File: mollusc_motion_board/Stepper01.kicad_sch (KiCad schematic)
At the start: 7 parts, among them J4 RJ45 x4, U1 SN74AHCT125N, U4 74HC14

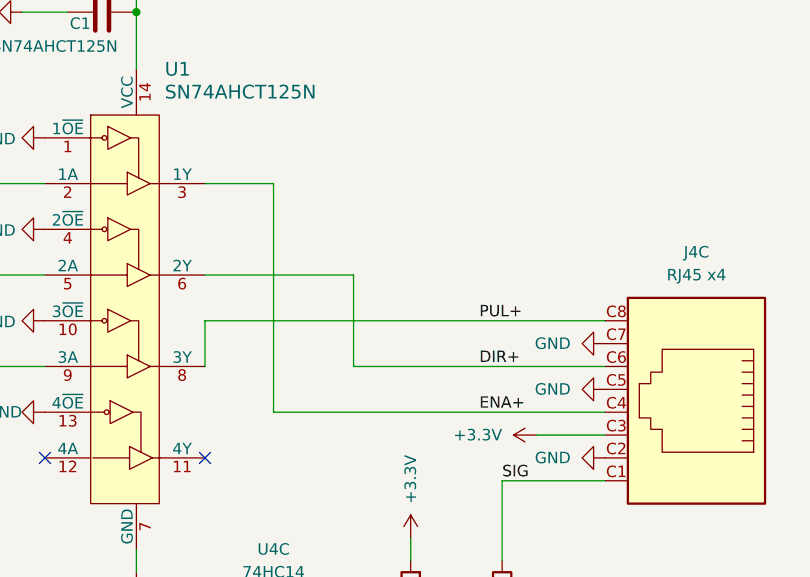
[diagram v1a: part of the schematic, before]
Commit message: adding ethernet jack
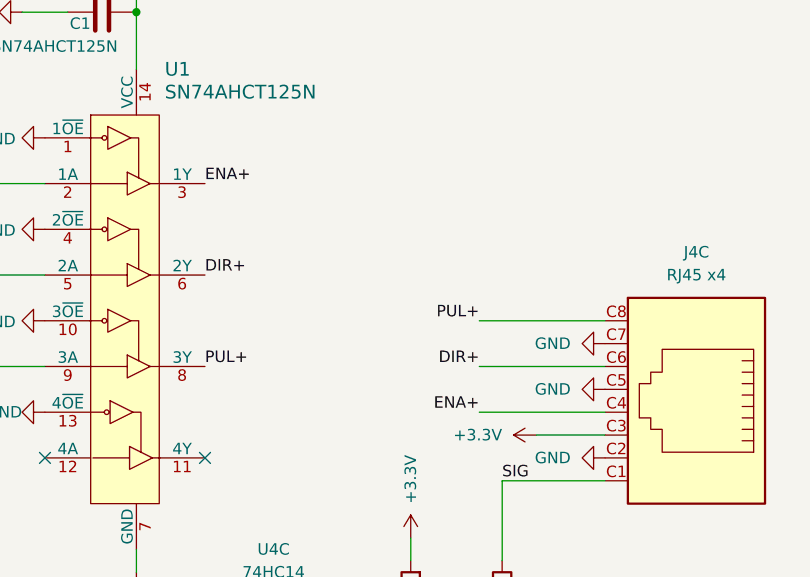
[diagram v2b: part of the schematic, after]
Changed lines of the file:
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@@
   (no_connect (at 166.37 107.95))
   (no_connect (at 148.59 107.95))
-  (wire (pts (xy 166.37 92.71) (xy 166.37 97.79))
-    (stroke (width 0) (type default))
-  )
   (wire (pts (xy 146.05 58.42) (xy 151.13 58.42))
-    (stroke (width 0) (type default))
-  )
-  (wire (pts (xy 173.99 102.87) (xy 210.82 102.87))
     (stroke (width 0) (type default))
   )
@@
     (stroke (width 0) (type default))
   )
+  (wire (pts (xy 196.85 97.79) (xy 210.82 97.79))
+    (stroke (width 0) (type default))
+  )
   (wire (pts (xy 138.43 87.63) (xy 148.59 87.63))
+    (stroke (width 0) (type default))
+  )
+  (wire (pts (xy 196.85 92.71) (xy 210.82 92.71))
     (stroke (width 0) (type default))
   )
@@
     (stroke (width 0) (type default))
   )
-  (wire (pts (xy 173.99 102.87) (xy 173.99 77.47))
+  (wire (pts (xy 196.85 102.87) (xy 210.82 102.87))
     (stroke (width 0) (type default))
   )
@@
     (stroke (width 0) (type default))
   )
-  (wire (pts (xy 166.37 77.47) (xy 173.99 77.47))
-    (stroke (width 0) (type default))
-  )
   (wire (pts (xy 199.39 110.49) (xy 199.39 119.38))
-    (stroke (width 0) (type default))
-  )
-  (wire (pts (xy 166.37 92.71) (xy 210.82 92.71))
-    (stroke (width 0) (type default))
-  )
-  (wire (pts (xy 182.88 97.79) (xy 210.82 97.79))
-    (stroke (width 0) (type default))
-  )
-  (wire (pts (xy 182.88 87.63) (xy 182.88 97.79))
-    (stroke (width 0) (type default))
-  )
-  (wire (pts (xy 166.37 87.63) (xy 182.88 87.63))
     (stroke (width 0) (type default))
   )
@@
     (effects (font (size 5.08 5.08)) (justify left bottom))
   )
-  (label "DIR+" (at 196.85 97.79 0) (fields_autoplaced)
-    (effects (font (size 1.27 1.27)) (justify left bottom))
+  (label "DIR+" (at 196.85 97.79 180) (fields_autoplaced)
+    (effects (font (size 1.27 1.27)) (justify right bottom))
   )
-  (label "ENA+" (at 196.85 102.87 0) (fields_autoplaced)
+  (label "ENA+" (at 196.85 102.87 180) (fields_autoplaced)
+    (effects (font (size 1.27 1.27)) (justify right bottom))
+  )
+  (label "DIR+" (at 166.37 87.63 0) (fields_autoplaced)
     (effects (font (size 1.27 1.27)) (justify left bottom))
   )
@@
     (effects (font (size 1.27 1.27)) (justify left bottom))
   )
-  (label "PUL+" (at 196.85 92.71 0) (fields_autoplaced)
+  (label "PUL+" (at 166.37 97.79 0) (fields_autoplaced)
     (effects (font (size 1.27 1.27)) (justify left bottom))
   )
+  (label "ENA+" (at 166.37 77.47 0) (fields_autoplaced)
+    (effects (font (size 1.27 1.27)) (justify left bottom))
+  )
+  (label "PUL+" (at 196.85 92.71 180) (fields_autoplaced)
+    (effects (font (size 1.27 1.27)) (justify right bottom))
+  )
   (hierarchical_label "Stepper_ENABLE" (shape input) (at 138.43 77.47 180) (fields_autoplaced)

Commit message: Board v2 wip
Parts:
- C1, C3: value 0.1uF 16V -> 0.1uF 50V; footprint HangOn_Mainboard:R0603 -> molluscmotion:C0603
- R1, R2: footprint HangOn_Mainboard:R0603 -> molluscmotion:R0603
- U1, U4: footprint HangOn_Mainboard:SOIC-14_L8.7-W3.9-P1.27-LS6.0-BL -> molluscmotion:SOIC-14_L8.7-W3.9-P1.27-LS6.0-BL
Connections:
- net +3.3V: now also J4.D3; no longer J4.C3
- net DIR+: now also J4.D6; no longer J4.C6
- net ENA+: now also J4.D4; no longer J4.C4
- net GND: now also J4.D2, J4.D5, J4.D7; no longer J4.C2, J4.C5, J4.C7
- net PUL+: now also J4.D8; no longer J4.C8
- net SIG: now also J4.D1; no longer J4.C1
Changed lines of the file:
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@@
       (effects (font (size 1.27 1.27)) (justify right))
     )
-    (property "Footprint" "HangOn_Mainboard:R0603" (at 191.008 123.19 90)
+    (property "Footprint" "molluscmotion:R0603" (at 191.008 123.19 90)
       (effects (font (size 1.27 1.27)) hide)
     )
@@
     )
   )
-  (symbol (lib_id "clockdiv:RJ45_x4") (at 213.36 101.6 0) (mirror y) (unit 3)
+  (symbol (lib_id "clockdiv:RJ45_x4") (at 213.36 101.6 0) (mirror y) (unit 4)
     (in_bom yes) (on_board yes) (dnp no) (fields_autoplaced)
     (property "Reference" "J4" (at 220.98 85.09 0)
@@
       (project "mollusc_motion_board"
         (path "/351cebb8-982f-46d7-8218-395788e5ce03/679b5948-2929-4082-9ec3-0ebae5348a76"
-          (reference "J4") (unit 3)
+          (reference "J4") (unit 4)
         )
       )
@@
       (effects (font (size 1.524 1.524)) (justify left))
     )
-    (property "Footprint" "HangOn_Mainboard:SOIC-14_L8.7-W3.9-P1.27-LS6.0-BL" (at 163.83 77.47 0)
+    (property "Footprint" "molluscmotion:SOIC-14_L8.7-W3.9-P1.27-LS6.0-BL" (at 163.83 77.47 0)
       (effects (font (size 1.524 1.524)) (justify left) hide)
     )
@@
       (effects (font (size 1.27 1.27)))
     )
-    (property "Footprint" "HangOn_Mainboard:SOIC-14_L8.7-W3.9-P1.27-LS6.0-BL" (at 173.99 127 0)
+    (property "Footprint" "molluscmotion:SOIC-14_L8.7-W3.9-P1.27-LS6.0-BL" (at 173.99 127 0)
       (effects (font (size 1.27 1.27)) hide)
     )
@@
       (effects (font (size 1.27 1.27)) (justify left))
     )
-    (property "Footprint" "HangOn_Mainboard:R0603" (at 197.612 123.19 90)
+    (property "Footprint" "molluscmotion:R0603" (at 197.612 123.19 90)
       (effects (font (size 1.27 1.27)) hide)
     )
@@
       (effects (font (size 1.27 1.27)) (justify left))
     )
-    (property "Value" "0.1uF 16V" (at 192.151 131.953 0)
-      (effects (font (size 1.27 1.27)) (justify left))
-    )
-    (property "Footprint" "HangOn_Mainboard:R0603" (at 190.1952 134.62 0)
+    (property "Value" "0.1uF 50V " (at 192.151 131.953 0)
+      (effects (font (size 1.27 1.27)) (justify left))
+    )
+    (property "Footprint" "molluscmotion:C0603" (at 190.1952 134.62 0)
       (effects (font (size 1.27 1.27)) hide)
     )
@@
       (effects (font (size 1.27 1.27)) (justify left))
     )
-    (property "Value" "0.1uF 16V " (at 157.48 54.61 90)
-      (effects (font (size 1.27 1.27)) (justify left))
-    )
-    (property "Footprint" "HangOn_Mainboard:R0603" (at 158.75 57.4548 0)
-      (effects (font (size 1.27 1.27)) hide)
-    )
+    (property "Value" "0.1uF 50V " (at 157.48 54.61 90)
+      (effects (font (size 1.27 1.27)) (justify left))
+    )
+    (property "Footprint" "molluscmotion:C0603" (at 158.75 57.4548 0)
+      (effects (font (size 1.27 1.27)) hide)
+    )

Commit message: PCB v1.2 Layout
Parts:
- added D5: ESD5Z5_0T1G, molluscmotion:SOD-523F_L1.2-W0.8-LS1.7-RD, symbol molluscmotion:ESD5Z5_0T1G
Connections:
- net GND: now also D5.2 (A)
- net at C3.1, R1.1, R2.2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: now also D5.1 (C)
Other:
- moved on the sheet: R1, R2
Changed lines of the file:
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@@
 (kicad_sch (version 20230121) (generator eeschema)
   (paper "A4")
+  (junction (at 199.39 127) (diameter 0) (color 0 0 0 0)
+  )
   (junction (at 158.75 58.42) (diameter 0) (color 0 0 0 0)
   )
   (junction (at 189.23 127) (diameter 0) (color 0 0 0 0)
+  )
+  (junction (at 194.31 138.43) (diameter 0) (color 0 0 0 0)
   )
   (no_connect (at 166.37 107.95))
@@
     (stroke (width 0) (type default))
   )
-  (wire (pts (xy 189.23 127) (xy 199.39 127))
-    (stroke (width 0) (type default))
-  )
   (wire (pts (xy 196.85 102.87) (xy 210.82 102.87))
     (stroke (width 0) (type default))
   )
-  (wire (pts (xy 189.23 116.84) (xy 189.23 119.38))
+  (wire (pts (xy 199.39 137.16) (xy 199.39 138.43))
+    (stroke (width 0) (type default))
+  )
+  (wire (pts (xy 199.39 127) (xy 189.23 127))
+    (stroke (width 0) (type default))
+  )
+  (wire (pts (xy 189.23 116.84) (xy 189.23 118.11))
     (stroke (width 0) (type default))
   )
@@
     (stroke (width 0) (type default))
   )
-  (wire (pts (xy 199.39 110.49) (xy 199.39 119.38))
+  (wire (pts (xy 199.39 110.49) (xy 199.39 114.3))
+    (stroke (width 0) (type default))
+  )
+  (wire (pts (xy 199.39 127) (xy 199.39 121.92))
+    (stroke (width 0) (type default))
+  )
+  (wire (pts (xy 194.31 138.43) (xy 194.31 140.97))
+    (stroke (width 0) (type default))
+  )
+  (wire (pts (xy 189.23 134.62) (xy 189.23 138.43))
+    (stroke (width 0) (type default))
+  )
+  (wire (pts (xy 189.23 125.73) (xy 189.23 127))
+    (stroke (width 0) (type default))
+  )
+  (wire (pts (xy 194.31 138.43) (xy 199.39 138.43))
+    (stroke (width 0) (type default))
+  )
+  (wire (pts (xy 189.23 138.43) (xy 194.31 138.43))
     (stroke (width 0) (type default))
   )
@@
     )
   )
-  (symbol (lib_id "Device:R") (at 189.23 123.19 180) (unit 1)
-    (in_bom yes) (on_board yes) (dnp no)
-    (property "Reference" "R1" (at 191.008 122.0216 0)
-      (effects (font (size 1.27 1.27)) (justify right))
-    )
-    (property "Value" "10k" (at 191.008 124.333 0)
-      (effects (font (size 1.27 1.27)) (justify right))
-    )
-    (property "Footprint" "molluscmotion:R0603" (at 191.008 123.19 90)
-      (effects (font (size 1.27 1.27)) hide)
-    )
-    (property "Datasheet" "~" (at 189.23 123.19 0)
-      (effects (font (size 1.27 1.27)) hide)
-    )
-    (property "JLCPCB Part #" "C25804" (at 189.23 123.19 0)
+  (symbol (lib_id "Device:R") (at 189.23 121.92 180) (unit 1)
+    (in_bom yes) (on_board yes) (dnp no)
+    (property "Reference" "R1" (at 191.008 120.7516 0)
+      (effects (font (size 1.27 1.27)) (justify right))
+    )
+    (property "Value" "10k" (at 191.008 123.063 0)
+      (effects (font (size 1.27 1.27)) (justify right))
+    )
+    (property "Footprint" "molluscmotion:R0603" (at 191.008 121.92 90)
+      (effects (font (size 1.27 1.27)) hide)
+    )
+    (property "Datasheet" "~" (at 189.23 121.92 0)
+      (effects (font (size 1.27 1.27)) hide)
+    )
+    (property "JLCPCB Part #" "C25804" (at 189.23 121.92 0)
       (effects (font (size 1.27 1.27)) hide)
     )
@@
     )
   )
-  (symbol (lib_id "Device:R") (at 199.39 123.19 0) (unit 1)
-    (in_bom yes) (on_board yes) (dnp no)
-    (property "Reference" "R2" (at 201.168 122.0216 0)
+  (symbol (lib_id "Device:R") (at 199.39 118.11 0) (unit 1)
+    (in_bom yes) (on_board yes) (dnp no)
+    (property "Reference" "R2" (at 201.168 116.9416 0)
       (effects (font (size 1.27 1.27)) (justify left))
     )
-    (property "Value" "1k" (at 201.168 124.333 0)
+    (property "Value" "1k" (at 201.168 119.253 0)
       (effects (font (size 1.27 1.27)) (justify left))
     )
-    (property "Footprint" "molluscmotion:R0603" (at 197.612 123.19 90)
-      (effects (font (size 1.27 1.27)) hide)
-    )
-    (property "Datasheet" "~" (at 199.39 123.19 0)
-      (effects (font (size 1.27 1.27)) hide)
-    )
-    (property "JLCPCB Part #" "C21190" (at 199.39 123.19 0)
+    (property "Footprint" "molluscmotion:R0603" (at 197.612 118.11 90)
+      (effects (font (size 1.27 1.27)) hide)
+    )
+    (property "Datasheet" "~" (at 199.39 118.11 0)
+      (effects (font (size 1.27 1.27)) hide)
+    )
+    (property "JLCPCB Part #" "C21190" (at 199.39 118.11 0)
       (effects (font (size 1.27 1.27)) hide)
     )
@@
     )
   )
+  (symbol (lib_id "molluscmotion:ESD5Z5_0T1G") (at 199.39 132.08 270) (unit 1)
+    (in_bom yes) (on_board yes) (dnp no)
+    (property "Reference" "D5" (at 203.2 133.35 90)
+      (effects (font (size 1.27 1.27)))
+    )
+    (property "Value" "ESD5Z5_0T1G" (at 207.01 135.89 90)
+      (effects (font (size 1.27 1.27)))
+    )
+    (property "Footprint" "molluscmotion:SOD-523F_L1.2-W0.8-LS1.7-RD" (at 189.23 132.08 0)
+      (effects (font (size 1.27 1.27) italic) hide)
+    )
+    (property "Datasheet" "https://item.szlcsc.com/235389.html" (at 199.517 129.794 0)
+      (effects (font (size 1.27 1.27)) (justify left) hide)
+    )
+    (property "LCSC" "C82044" (at 199.39 132.08 0)
+      (effects (font (size 1.27 1.27)) hide)
+    )
+    (pin "1")
+    (pin "2")
+    (instances
+      (project "mollusc_motion_board"
+        (path "/351cebb8-982f-46d7-8218-395788e5ce03/679b5948-2929-4082-9ec3-0ebae5348a76"
+          (reference "D5") (unit 1)
+        )
+      )
+    )
+  )
   (symbol (lib_id "power:GND") (at 148.59 72.39 270) (unit 1)
     (in_bom yes) (on_board yes) (dnp no)
@@
   (symbol (lib_id "Device:C") (at 189.23 130.81 0) (unit 1)
     (in_bom yes) (on_board yes) (dnp no)
-    (property "Reference" "C3" (at 192.151 129.6416 0)
+    (property "Reference" "C3" (at 184.15 130.81 0)
       (effects (font (size 1.27 1.27)) (justify left))
     )
-    (property "Value" "0.1uF 50V " (at 192.151 131.953 0)
+    (property "Value" "0.1uF 50V " (at 179.07 133.35 0)
       (effects (font (size 1.27 1.27)) (justify left))
     )
@@
     )
   )
-  (symbol (lib_id "power:GND") (at 189.23 134.62 0) (unit 1)
-    (in_bom yes) (on_board yes) (dnp no)
-    (property "Reference" "#PWR07" (at 189.23 140.97 0)
-      (effects (font (size 1.27 1.27)) hide)
-    )
-    (property "Value" "GND" (at 187.96 135.89 0)
-      (effects (font (size 1.27 1.27)) (justify right))
-    )
-    (property "Footprint" "" (at 189.23 134.62 0)
-      (effects (font (size 1.27 1.27)) hide)
-    )
-    (property "Datasheet" "" (at 189.23 134.62 0)
-      (effects (font (size 1.27 1.27)) hide)
-    )
+  (symbol (lib_id "power:GND") (at 194.31 140.97 0) (unit 1)
+    (in_bom yes) (on_board yes) (dnp no)
+    (property "Reference" "#PWR07" (at 194.31 147.32 0)
+      (effects (font (size 1.27 1.27)) hide)
+    )
+    (property "Value" "GND" (at 196.85 144.78 0)
+      (effects (font (size 1.27 1.27)) (justify right))
+    )
+    (property "Footprint" "" (at 194.31 140.97 0)
+      (effects (font (size 1.27 1.27)) hide)
+    )
+    (property "Datasheet" "" (at 194.31 140.97 0)
+      (effects (font (size 1.27 1.27)) hide)
+    )
